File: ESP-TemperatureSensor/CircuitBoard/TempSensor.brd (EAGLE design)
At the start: 26.7 x 47 mm, 12 parts

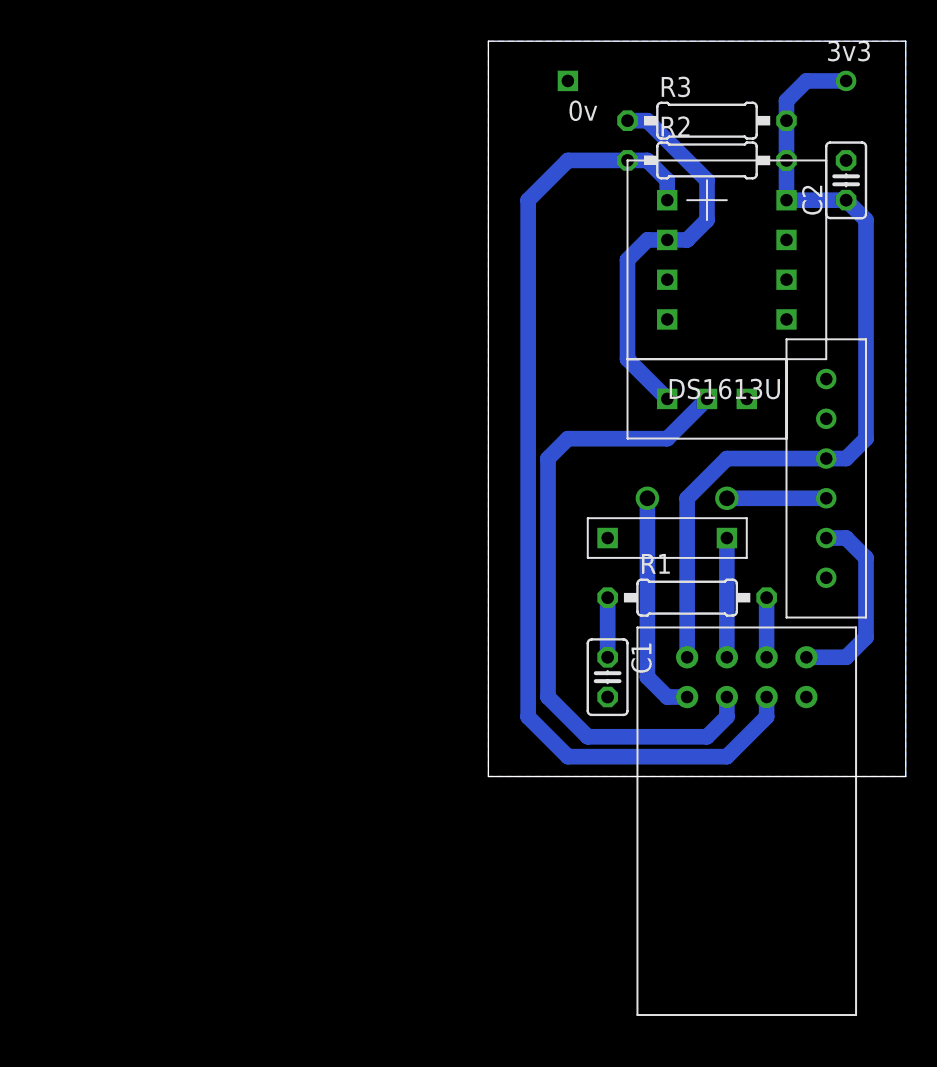
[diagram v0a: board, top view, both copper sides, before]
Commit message: Fixing issue with board upload
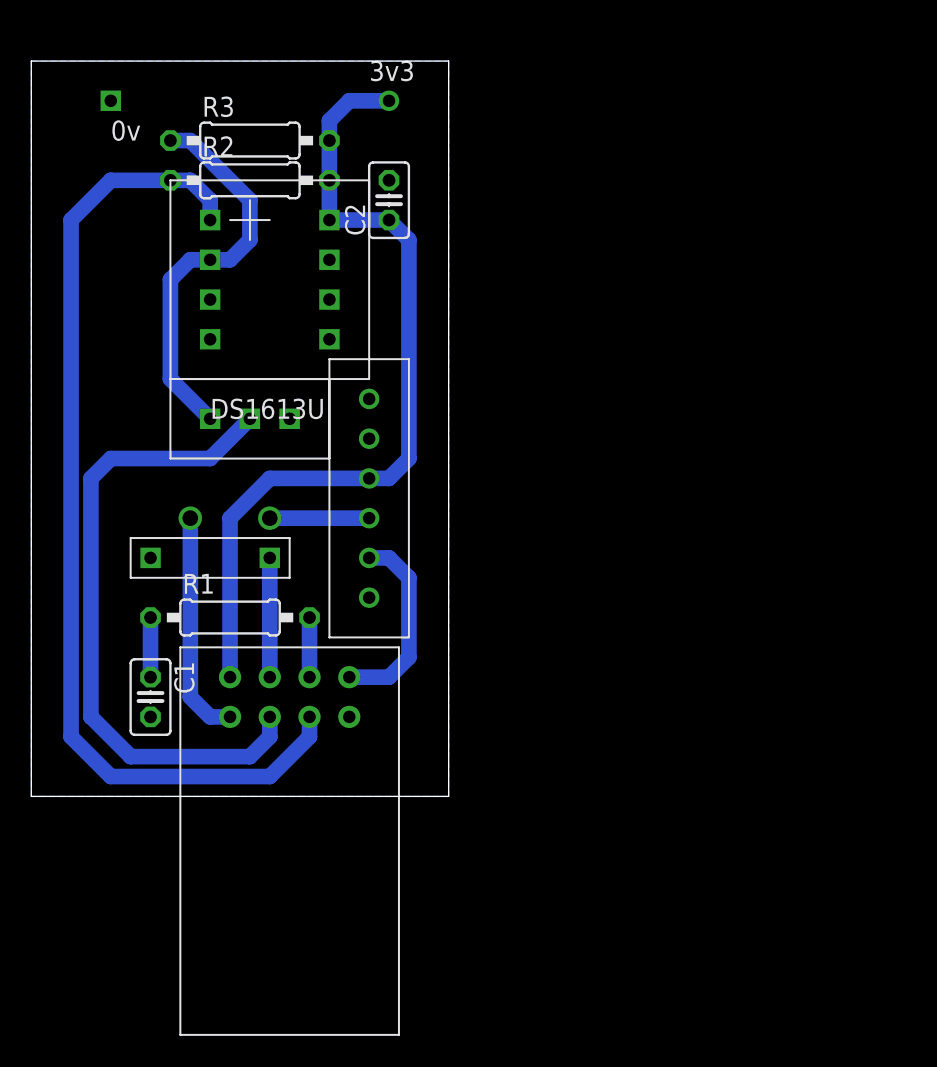
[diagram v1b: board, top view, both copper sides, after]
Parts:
- moved U$1 29.2 mm to (36.8, 22.9)
- moved C1 29.2 mm to (24.1, 21.6)
- moved C2 29.2 mm to (39.4, 53.3)
- moved R1 29.2 mm to (29.2, 26.7)
- moved U$2 29.2 mm to (29.2, 30.5)
- moved U$5 29.2 mm to (38.1, 38.1)
- moved U$6 29.2 mm to (39.4, 59.7)
- moved R2 29.2 mm to (30.5, 54.6)
- moved R3 29.2 mm to (30.5, 57.1)
- moved U$4 29.2 mm to (30.5, 39.4)
- moved U$7 29.2 mm to (21.6, 59.7)
- moved U$3 29.2 mm to (33.0, 49.5)

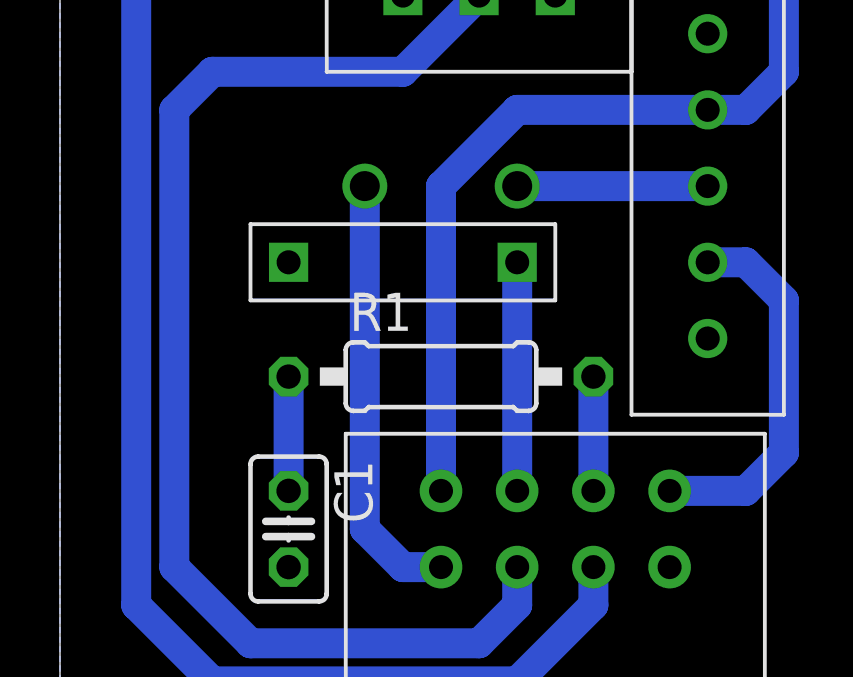
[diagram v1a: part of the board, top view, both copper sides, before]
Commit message: Updated the circuit
Updated the circuit diagram and created a better single sided PCB design
for prototyping.
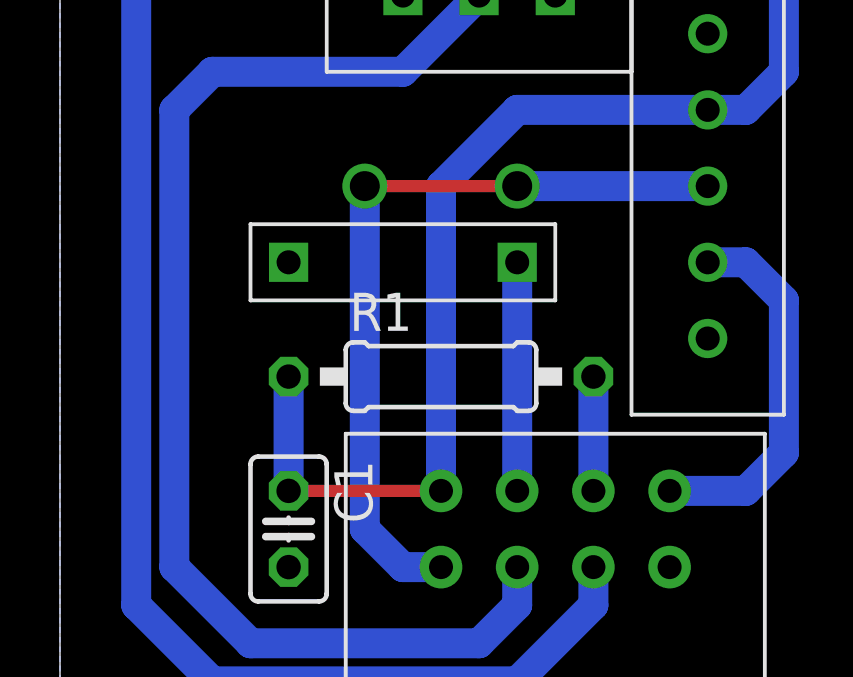
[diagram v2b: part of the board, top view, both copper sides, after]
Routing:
- net N$5: track 20.8 -> 25.9 mm
- net +3V3: track 57.2 -> 62.3 mm
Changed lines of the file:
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@@
 <?xml version="1.0" encoding="utf-8"?>
 <!DOCTYPE eagle SYSTEM "eagle.dtd">
-<eagle version="7.1.0">
+<eagle version="7.2.0">
 <drawing>
 <settings>
@@
 <wire x1="35.56" y1="54.61" x2="35.56" y2="52.07" width="1" layer="16"/>
 <wire x1="35.56" y1="57.15" x2="35.56" y2="54.61" width="1" layer="16"/>
-<wire x1="24.13" y1="22.86" x2="29.21" y2="22.86" width="0" layer="19" extent="1-1"/>
+<wire x1="24.13" y1="22.86" x2="29.21" y2="22.86" width="0.4064" layer="1"/>
 </signal>
 <signal name="GND">
@@
 <via x="31.75" y="33.02" extent="1-16" drill="1"/>
 <wire x1="31.75" y1="33.02" x2="38.1" y2="33.02" width="1" layer="16"/>
-<wire x1="26.67" y1="33.02" x2="31.75" y2="33.02" width="0" layer="19" extent="1-1"/>
+<wire x1="31.75" y1="33.02" x2="26.67" y2="33.02" width="0.4064" layer="1"/>
 </signal>
 <signal name="N$6">
